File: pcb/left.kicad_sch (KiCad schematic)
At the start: 111 parts, among them J101 PJ-320A, SW101 =, SW102 1, SW103 2, SW104 3, SW105 4, SW106 5, SW107 Tab, SW108 Q, SW109 W, SW110 E, SW111 R, SW112 T, SW113 Esc, SW114 A, SW115 S, SW116 D, SW117 F, SW118 G, SW119 Alt, SW120 Shift, SW121 Z, SW122 X, SW123 C, SW124 V, SW125 B, SW126 Ctrl, SW127 `, SW128 Caps, SW129 Left, SW130 Right, SW131 Super, SW132 Bksp, SW133 Del, SW190 MSK12C02 power, SW191 Reset, U101 nRF52840 Pro Micro

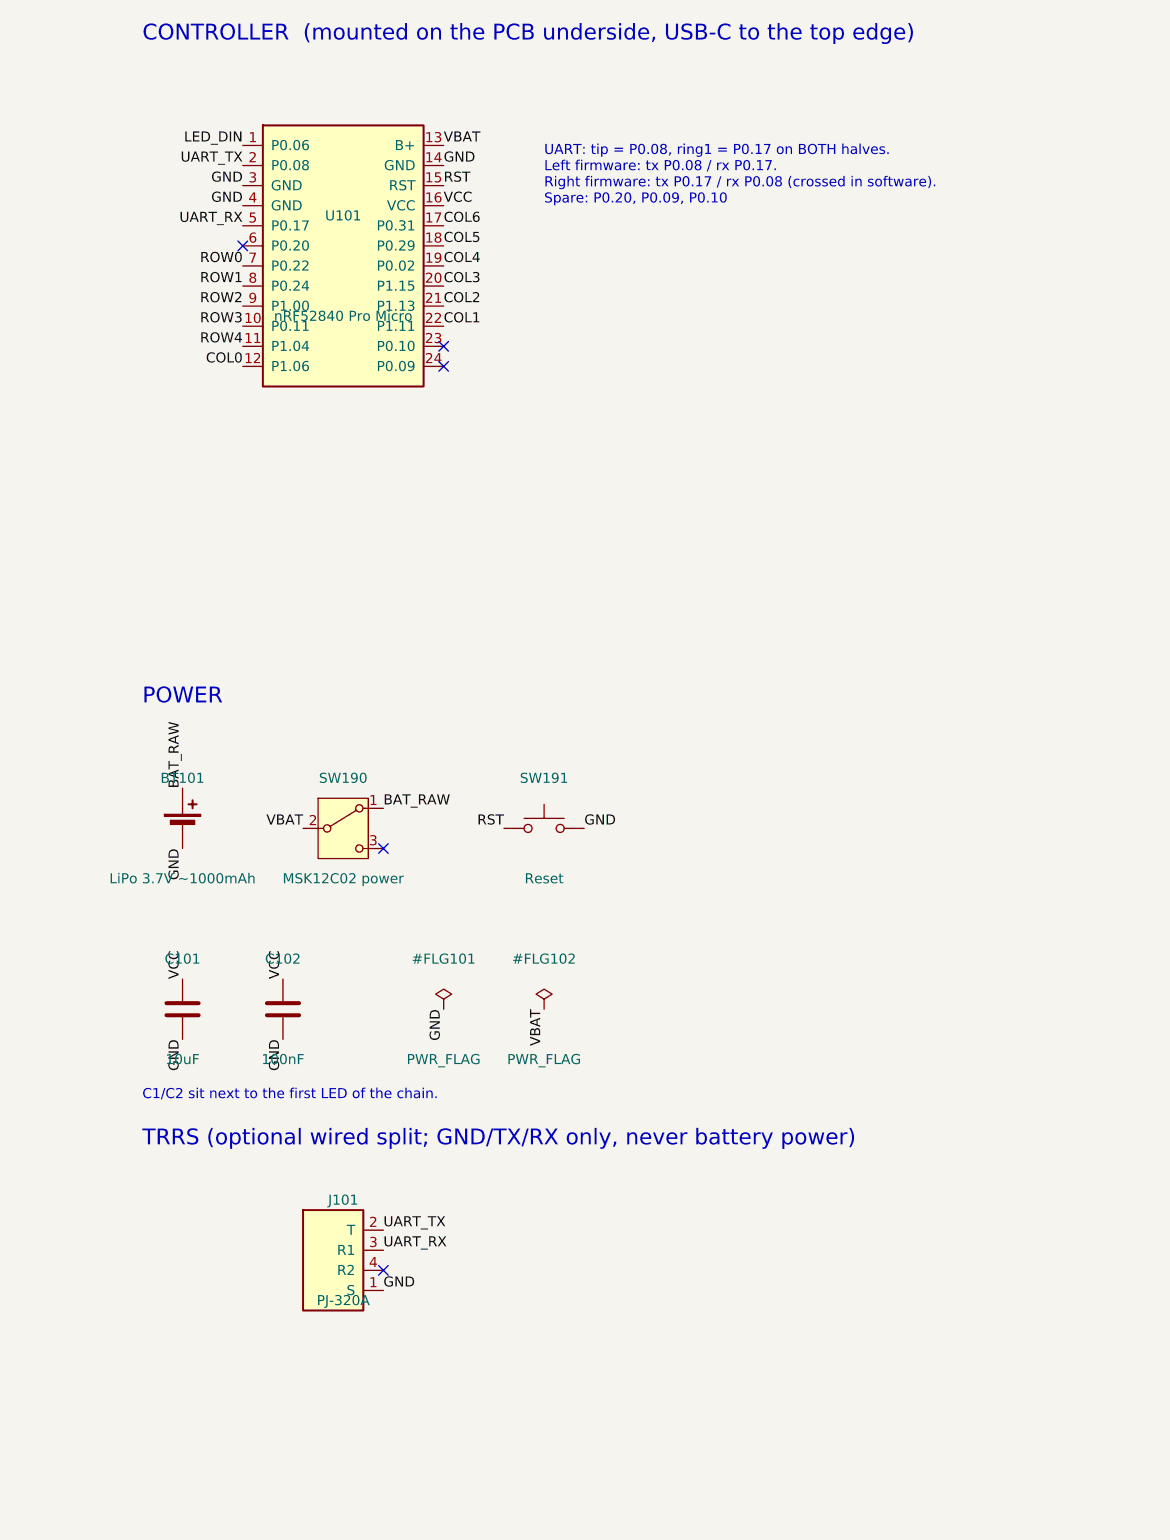
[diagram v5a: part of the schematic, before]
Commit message: Drop the TRRS jack and switch the battery through a MOSFET
Settle power and connectivity before ordering. The halves talk over
Bluetooth only; USB-C on the left half is the wired mode. The TRRS jack
would only have replaced the Bluetooth split, needs its own ZMK build,
can't charge the other half (the nice!nano has no VBUS pin) and must not
be hot-plugged while a half is powered, which with a battery in each half
is always. P0.08 and P0.17 become spare.

The genuine nice!nano v2 charges at 500 mA with BOOST bridged, but the
MSK12C02 slide switch is rated 50 mA. It now only drives the gate of an
AO3401A P-MOSFET (source on the battery, drain on B+) with a 1 MOhm gate
resistor, so no battery current passes through its contacts. The lever and
case opening are unchanged.

Battery: a pouch up to 5 mm thick, 1000-1500 mAh, lying over the hotswap
sockets under the inner columns, inside the depth the socketed controller
already needs.

DRC with schematic parity: 0 errors, 0 unconnected, 0 parity issues.
Datasheet audit: 85 pass, 8 warn, 0 fail.
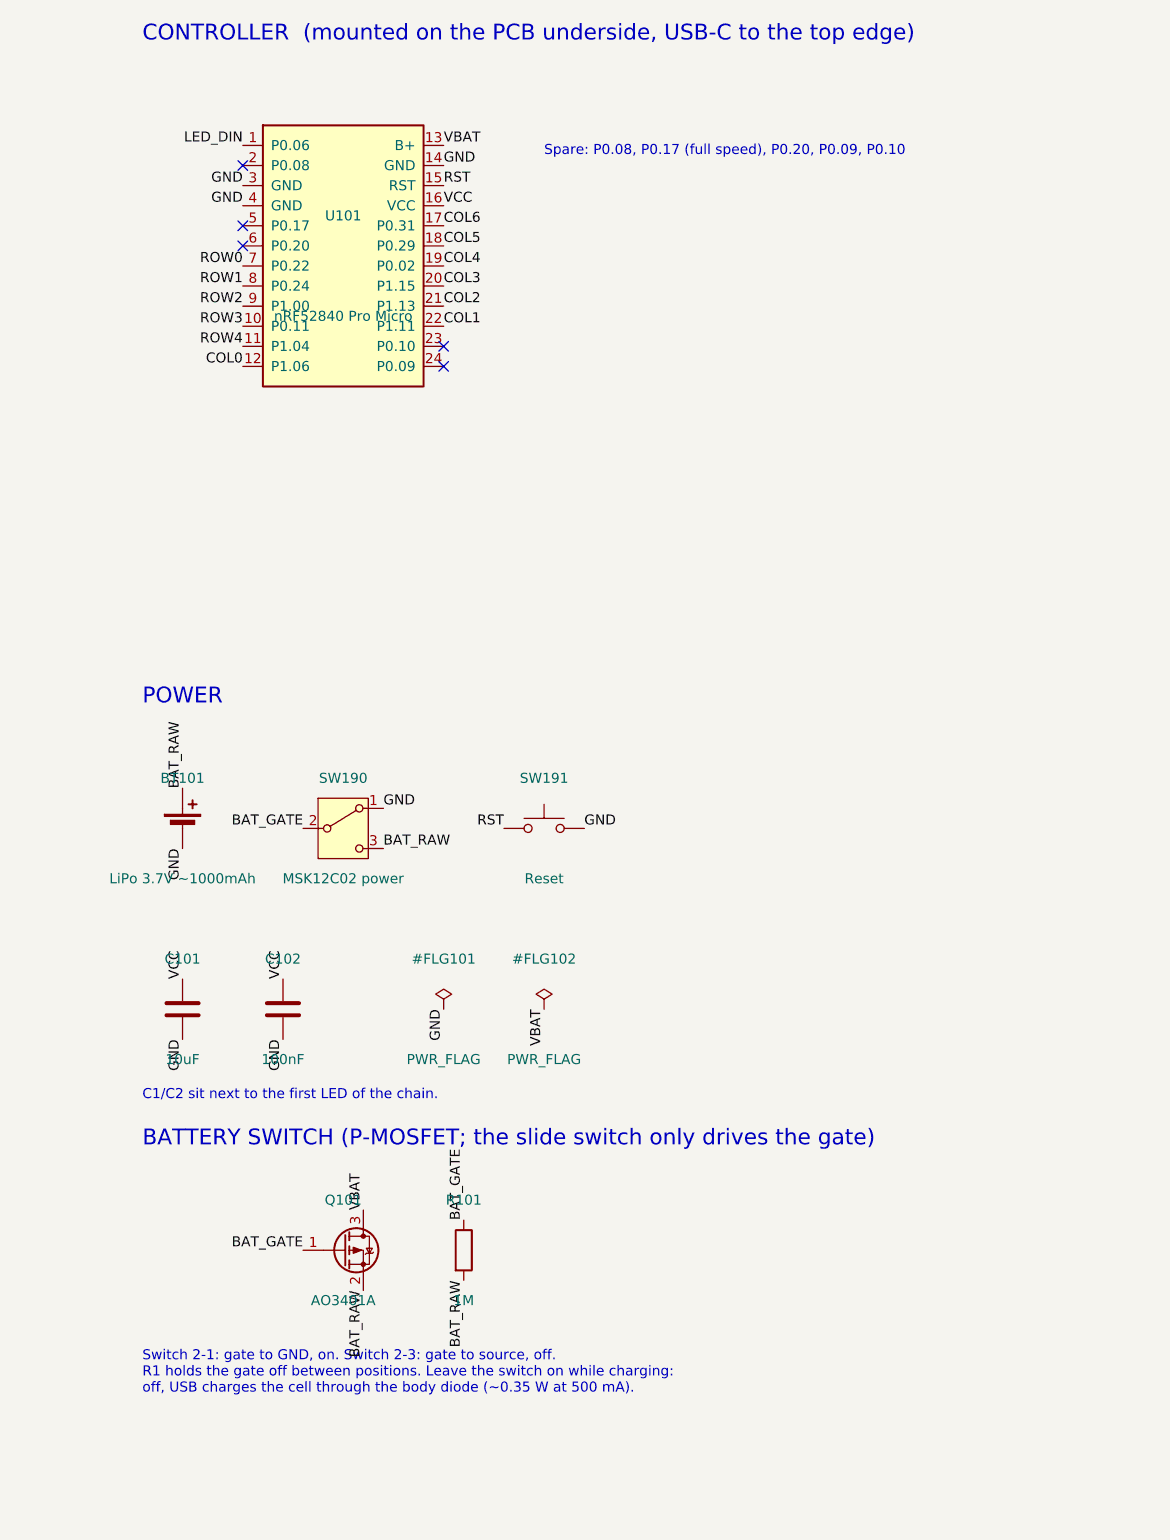
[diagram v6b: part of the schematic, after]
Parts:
- removed J101: PJ-320A, keygen:TRRS-PJ-320A, symbol keygen:TRRS_PJ-320A
- added Q101: AO3401A, Package_TO_SOT_SMD:SOT-23, symbol Transistor_FET:AO3401A
- added R101: 1M, Resistor_SMD:R_0805_2012Metric, symbol Device:R
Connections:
- net BAT_RAW: now also SW190.3 (C), Q101.2 (S), R101.2; no longer SW190.1 (A)
- net GND: now also SW190.1 (A)
- net VBAT: now also Q101.3 (D); no longer SW190.2 (B)
- net UART_RX: no longer names the net of U101.5 (P0.17)
- net UART_TX: no longer names the net of U101.2 (P0.08)
- new net BAT_GATE: Q101.1 (G), R101.1, SW190.2 (B)
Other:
- note added: "BATTERY SWITCH (P-MOSFET; the slide switch only drives the gate)"
- note added: "Spare: P0.08, P0.17 (full speed), P0.20, P0.09, P0.10"
- note added: "Switch 2-1: gate to GND, on. Switch 2-3: gate to source, off. R1 holds the gate off between positions. Leave the switch on while charging: off, USB charges the cell through the body diode (~0.35 W at 500 mA)."
- note removed: "TRRS (optional wired split; GND/TX/RX only, never battery power)"
- note removed: "UART: tip = P0.08, ring1 = P0.17 on BOTH halves. Left firmware: tx P0.08 / rx P0.17. Right firmware: tx P0.17 / rx P0.08 (crossed in software). Spare: P0.20, P0.09, P0.10"
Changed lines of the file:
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@@
     (effects (font (size 1.27 1.27)) (justify right bottom))
   )
-  (label "UART_TX"
-    (at 347.98 48.26 180)
-    (effects (font (size 1.27 1.27)) (justify right bottom))
-  )
+  (no_connect (at 347.98 48.26))
   (label "GND"
     (at 347.98 50.8 180)
@@
     (effects (font (size 1.27 1.27)) (justify right bottom))
   )
-  (label "UART_RX"
-    (at 347.98 55.88 180)
-    (effects (font (size 1.27 1.27)) (justify right bottom))
-  )
+  (no_connect (at 347.98 55.88))
   (no_connect (at 347.98 58.42))
   (label "ROW0"
@@
   (no_connect (at 373.38 71.12))
   (no_connect (at 373.38 73.66))
-  (text "UART: tip = P0.08, ring1 = P0.17 on BOTH halves.\nLeft firmware: tx P0.08 / rx P0.17.\nRight firmware: tx P0.17 / rx P0.08 (crossed in software).\nSpare: P0.20, P0.09, P0.10"
+  (text "Spare: P0.08, P0.17 (full speed), P0.20, P0.09, P0.10"
     (exclude_from_sim no)
     (at 386.08 45.72 0)
@@
     )
   )
+  (label "GND"
+    (at 365.76 129.54 0)
+    (effects (font (size 1.27 1.27)) (justify left bottom))
+  )
+  (label "BAT_GATE"
+    (at 355.6 132.08 180)
+    (effects (font (size 1.27 1.27)) (justify right bottom))
+  )
   (label "BAT_RAW"
-    (at 365.76 129.54 0)
-    (effects (font (size 1.27 1.27)) (justify left bottom))
-  )
-  (label "VBAT"
-    (at 355.6 132.08 180)
-    (effects (font (size 1.27 1.27)) (justify right bottom))
-  )
-  (no_connect (at 365.76 134.62))
+    (at 365.76 134.62 0)
+    (effects (font (size 1.27 1.27)) (justify left bottom))
+  )
   (symbol
     (lib_id "Switch:SW_Push")
@@
     (effects (font (size 1.27 1.27)) (justify left top))
   )
-  (text "TRRS (optional wired split; GND/TX/RX only, never battery power)"
+  (text "BATTERY SWITCH (P-MOSFET; the slide switch only drives the gate)"
     (exclude_from_sim no)
     (at 335.28 170.18 0)
@@
   )
   (symbol
-    (lib_id "keygen:TRRS_PJ-320A")
+    (lib_id "Transistor_FET:AO3401A")
     (at 360.68 185.42 0)
     (unit 1)
@@
     (on_board yes)
     (dnp no)
-    (property "Reference" "J101" (at 360.68 179.07 0) (effects (font (size 1.27 1.27))))
-    (property "Value" "PJ-320A" (at 360.68 191.77 0) (effects (font (size 1.27 1.27))))
-    (property "Footprint" "keygen:TRRS-PJ-320A"
+    (property "Reference" "Q101" (at 360.68 179.07 0) (effects (font (size 1.27 1.27))))
+    (property "Value" "AO3401A" (at 360.68 191.77 0) (effects (font (size 1.27 1.27))))
+    (property "Footprint" "Package_TO_SOT_SMD:SOT-23"
       (at 360.68 185.42 0)
       (effects (font (size 1.27 1.27)) (hide yes))
     )
     (property "Datasheet" "" (at 360.68 185.42 0) (effects (font (size 1.27 1.27)) (hide yes)))
+    (pin "1")
     (pin "2")
     (pin "3")
-    (pin "4")
-    (pin "1")
-    (instances
-      (project "keygen"
-        (path "/6967da33-a0e5-5fa7-9742-40725aff3c90/857ae29d-aaae-533f-894e-3d0d86c0d5f9"
-          (reference "J101")
-          (unit 1)
-        )
-      )
-    )
-  )
-  (label "UART_TX"
-    (at 365.76 182.88 0)
-    (effects (font (size 1.27 1.27)) (justify left bottom))
-  )
-  (label "UART_RX"
-    (at 365.76 185.42 0)
-    (effects (font (size 1.27 1.27)) (justify left bottom))
-  )
-  (no_connect (at 365.76 187.96))
-  (label "GND"
-    (at 365.76 190.5 0)
-    (effects (font (size 1.27 1.27)) (justify left bottom))
+    (instances
+      (project "keygen"
+        (path "/6967da33-a0e5-5fa7-9742-40725aff3c90/857ae29d-aaae-533f-894e-3d0d86c0d5f9"
+          (reference "Q101")
+          (unit 1)
+        )
+      )
+    )
+  )
+  (label "BAT_GATE"
+    (at 355.6 185.42 180)
+    (effects (font (size 1.27 1.27)) (justify right bottom))
+  )
+  (label "BAT_RAW"
+    (at 363.22 190.5 270)
+    (effects (font (size 1.27 1.27)) (justify right bottom))
+  )
+  (label "VBAT"
+    (at 363.22 180.34 90)
+    (effects (font (size 1.27 1.27)) (justify left bottom))
+  )
+  (symbol
+    (lib_id "Device:R")
+    (at 375.92 185.42 0)
+    (unit 1)
+    (exclude_from_sim no)
+    (in_bom yes)
+    (on_board yes)
+    (dnp no)
+    (property "Reference" "R101" (at 375.92 179.07 0) (effects (font (size 1.27 1.27))))
+    (property "Value" "1M" (at 375.92 191.77 0) (effects (font (size 1.27 1.27))))
+    (property "Footprint" "Resistor_SMD:R_0805_2012Metric"
+      (at 375.92 185.42 0)
+      (effects (font (size 1.27 1.27)) (hide yes))
+    )
+    (property "Datasheet" "" (at 375.92 185.42 0) (effects (font (size 1.27 1.27)) (hide yes)))
+    (pin "1")
+    (pin "2")
+    (instances
+      (project "keygen"
+        (path "/6967da33-a0e5-5fa7-9742-40725aff3c90/857ae29d-aaae-533f-894e-3d0d86c0d5f9"
+          (reference "R101")
+          (unit 1)
+        )
+      )
+    )
+  )
+  (label "BAT_GATE"
+    (at 375.92 181.61 90)
+    (effects (font (size 1.27 1.27)) (justify left bottom))
+  )
+  (label "BAT_RAW"
+    (at 375.92 189.23 270)
+    (effects (font (size 1.27 1.27)) (justify right bottom))
+  )
+  (text "Switch 2-1: gate to GND, on. Switch 2-3: gate to source, off.\nR1 holds the gate off between positions. Leave the switch on while charging:\noff, USB charges the cell through the body diode (~0.35 W at 500 mA)."
+    (exclude_from_sim no)
+    (at 335.28 198.12 0)
+    (effects (font (size 1.27 1.27)) (justify left top))
   )
   (text "MOUNTING HOLES (M2)"

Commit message: Power the LEDs from the battery through a MOSFET switch
The SK6812MINI-E is rated for VDD 3.7-5.5 V, and the nice!nano's 3.3 V
VCC has no published current limit for 33 LEDs. The LED rail (LED_VDD)
now runs from B+ through an AO3401A P-MOSFET (Q2). An AO3400A N-MOSFET
(Q3) on P0.08 pulls Q2's gate low to turn the LEDs on; 100 kOhm
resistors hold Q2 off (R2, gate to source) and Q3 off while the
controller boots or sleeps (R3). The 10 uF + 100 nF capacitors move to
Q2's output. VCC (pad 16) is unused. The cell is inside the LEDs'
rating until it runs low, and they light only on USB power.

All resistors and capacitors are now 1206 hand-solder footprints. The
new parts sit on the back between each battery connector and the board
edge, clear of the mounting holes, the antenna end and the top-edge
slot. They were added to the routed board, which was rerouted locally
with finish_route.py and smooth_route.py; the artwork was redrawn.

Firmware: ZMK's ext-power now drives P0.08 (and still P0.13, which only
switches the unused VCC). All three UF2 builds pass.

DRC with schematic parity: 0 errors, 0 unconnected, 0 parity; 14
silkscreen warnings. check_datasheets.py: 100 pass, 8 warn, 0 fail.
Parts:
- added Q102: AO3401A, Package_TO_SOT_SMD:SOT-23, symbol Transistor_FET:AO3401A
- added Q103: AO3400A, Package_TO_SOT_SMD:SOT-23, symbol Transistor_FET:AO3400A
- added R102, R103: 100k, Resistor_SMD:R_1206_3216Metric_Pad1.30x1.75mm_HandSolder, symbol Device:R
- BT101: value LiPo 3.7V ~1000mAh -> LiPo 3.7V 3000mAh
- C101, C102: footprint Capacitor_SMD:C_0805_2012Metric -> Capacitor_SMD:C_1206_3216Metric_Pad1.33x1.80mm_HandSolder
- R101: footprint Resistor_SMD:R_0805_2012Metric -> Resistor_SMD:R_1206_3216Metric_Pad1.30x1.75mm_HandSolder
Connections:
- net GND: now also Q103.2 (S), R103.2
- net VBAT: now also Q102.2 (S), R102.2
- net LED_EN: now reaches U101.2 (P0.08)
- net LED_EN: now also Q103.1 (G), R103.1
- net VCC renamed LED_VDD
- net LED_VDD: now also Q102.3 (D); no longer U101.16 (VCC)
- new net LED_GATE: Q102.1 (G), Q103.3 (D), R102.1
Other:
- note added: "C1/C2 sit at the LED power switch's output."
- note added: "LED POWER SWITCH (P0.08 high = LEDs on)"
- note added: "P0.08: LED power switch. VCC (pad 16) unused. Spare: P0.17 (full speed), P0.20, P0.09, P0.10"
- note added: "PER-KEY LEDs (33) - powered from the battery through the LED power switch (Q2, LED_VDD)"
- note removed: "C1/C2 sit next to the first LED of the chain."
- note removed: "PER-KEY LEDs (33, no underglow) - powered from the controller's switched VCC (P0.13); cap brightness in firmware"
- note removed: "Spare: P0.08, P0.17 (full speed), P0.20, P0.09, P0.10"
